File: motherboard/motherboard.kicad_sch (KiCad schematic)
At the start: 4 parts, among them J1 DF40C-100DP-0.4V(51), J2 DF40C-100DP-0.4V(51), J3 DF40C-100DP-0.4V(51), J4 DF40C-100DP-0.4V(51)

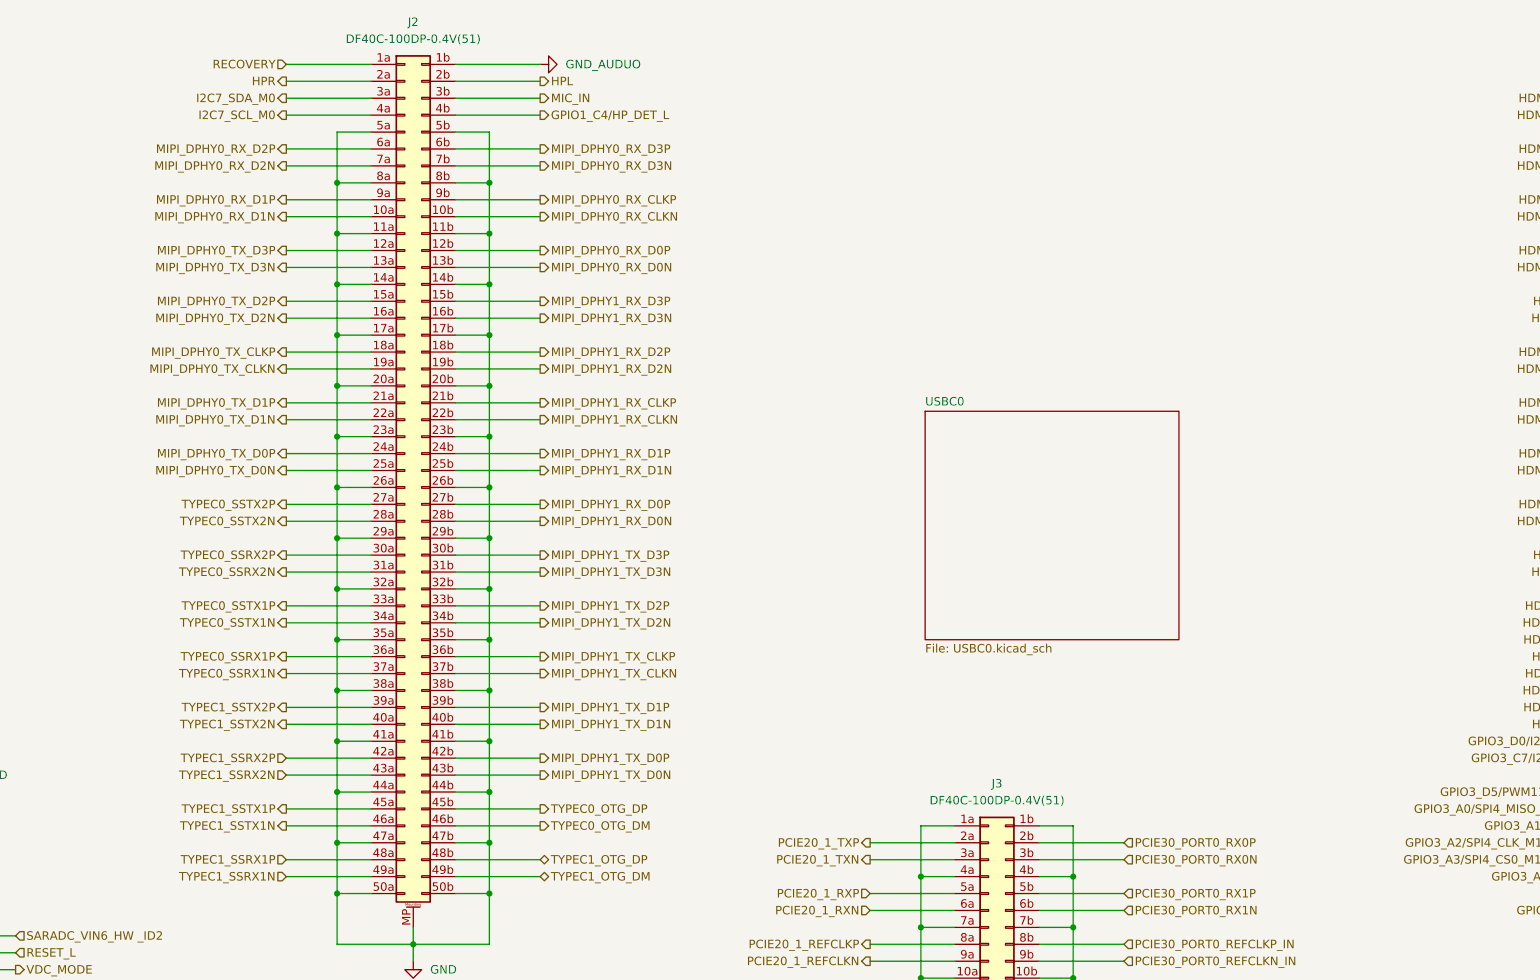
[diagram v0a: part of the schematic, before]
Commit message: hdmi, edp, peripheral implementations
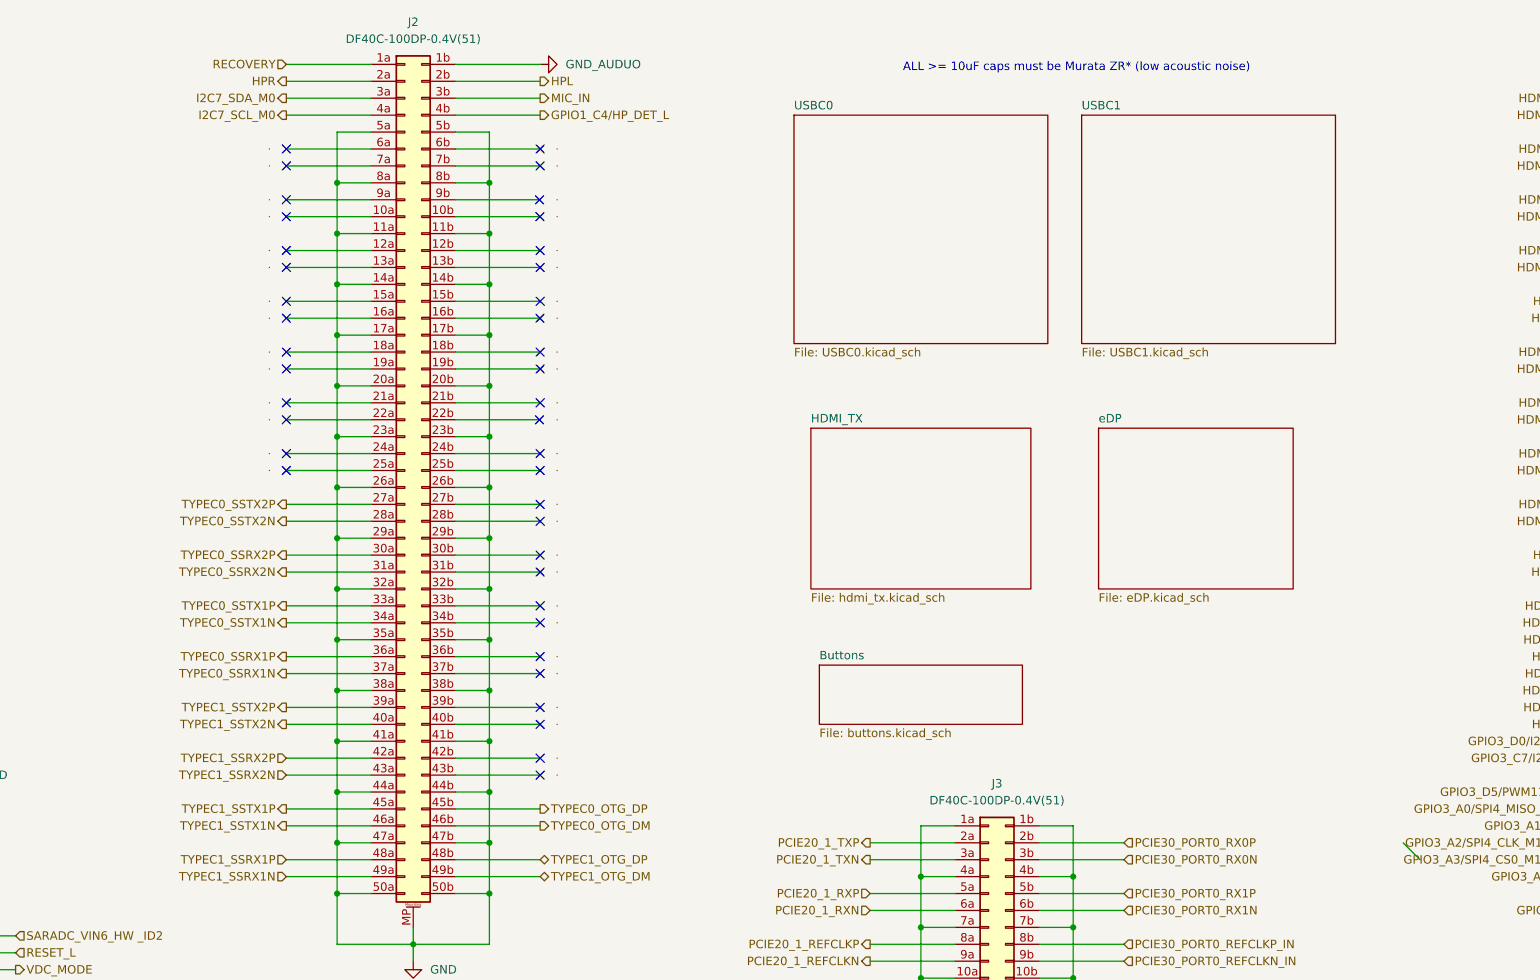
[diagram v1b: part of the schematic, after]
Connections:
- net MIPI_DPHY0_RX_CLKN: no longer J2.10b (Pin_10b)
- net MIPI_DPHY0_RX_CLKP: no longer J2.9b (Pin_9b)
- net MIPI_DPHY0_RX_D0N: no longer J2.13b (Pin_13b)
- net MIPI_DPHY0_RX_D0P: no longer J2.12b (Pin_12b)
- net MIPI_DPHY0_RX_D1N: no longer J2.10a (Pin_10a)
- net MIPI_DPHY0_RX_D1P: no longer J2.9a (Pin_9a)
- net MIPI_DPHY0_RX_D2N: no longer J2.7a (Pin_7a)
- net MIPI_DPHY0_RX_D2P: no longer J2.6a (Pin_6a)
- net MIPI_DPHY0_RX_D3N: no longer J2.7b (Pin_7b)
- net MIPI_DPHY0_RX_D3P: no longer J2.6b (Pin_6b)
- net MIPI_DPHY0_TX_CLKN: no longer J2.19a (Pin_19a)
- net MIPI_DPHY0_TX_CLKP: no longer J2.18a (Pin_18a)
- net MIPI_DPHY0_TX_D0N: no longer J2.25a (Pin_25a)
- net MIPI_DPHY0_TX_D0P: no longer J2.24a (Pin_24a)
- net MIPI_DPHY0_TX_D1N: no longer J2.22a (Pin_22a)
- net MIPI_DPHY0_TX_D1P: no longer J2.21a (Pin_21a)
- net MIPI_DPHY0_TX_D2N: no longer J2.16a (Pin_16a)
- net MIPI_DPHY0_TX_D2P: no longer J2.15a (Pin_15a)
- net MIPI_DPHY0_TX_D3N: no longer J2.13a (Pin_13a)
- net MIPI_DPHY0_TX_D3P: no longer J2.12a (Pin_12a)
- net MIPI_DPHY1_RX_CLKN: no longer J2.22b (Pin_22b)
- net MIPI_DPHY1_RX_CLKP: no longer J2.21b (Pin_21b)
- net MIPI_DPHY1_RX_D0N: no longer J2.28b (Pin_28b)
- net MIPI_DPHY1_RX_D0P: no longer J2.27b (Pin_27b)
- net MIPI_DPHY1_RX_D1N: no longer J2.25b (Pin_25b)
- net MIPI_DPHY1_RX_D1P: no longer J2.24b (Pin_24b)
- net MIPI_DPHY1_RX_D2N: no longer J2.19b (Pin_19b)
- net MIPI_DPHY1_RX_D2P: no longer J2.18b (Pin_18b)
- net MIPI_DPHY1_RX_D3N: no longer J2.16b (Pin_16b)
- net MIPI_DPHY1_RX_D3P: no longer J2.15b (Pin_15b)
- net MIPI_DPHY1_TX_CLKN: no longer J2.37b (Pin_37b)
- net MIPI_DPHY1_TX_CLKP: no longer J2.36b (Pin_36b)
- net MIPI_DPHY1_TX_D0N: no longer J2.43b (Pin_43b)
- net MIPI_DPHY1_TX_D0P: no longer J2.42b (Pin_42b)
- net MIPI_DPHY1_TX_D1N: no longer J2.40b (Pin_40b)
- net MIPI_DPHY1_TX_D1P: no longer J2.39b (Pin_39b)
- net MIPI_DPHY1_TX_D2N: no longer J2.34b (Pin_34b)
- net MIPI_DPHY1_TX_D2P: no longer J2.33b (Pin_33b)
- net MIPI_DPHY1_TX_D3N: no longer J2.31b (Pin_31b)
- net MIPI_DPHY1_TX_D3P: no longer J2.30b (Pin_30b)
- no-connect marks 0 -> 40
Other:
- added sheet Buttons (buttons.kicad_sch)
- added sheet HDMI_TX (hdmi_tx.kicad_sch)
- added sheet USBC1 (USBC1.kicad_sch)
- added sheet eDP (eDP.kicad_sch)
- note added: "ALL >= 10uF caps must be Murata ZR* (low acoustic noise)"
- company: (none) -> Byran Huang
- title: (none) -> anyon e

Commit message: wip with pcie2.0 e key, ethernet, buttons and more
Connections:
- net GPIO2_B) renamed GPIO2_B0
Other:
- added sheet Ethernet (ethernet.kicad_sch)
- added sheet PCIE2.0-EKEY (pcie20-ekey.kicad_sch)
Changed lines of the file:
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@@
 		(at 166.37 101.6)
 	)
-	(bus_entry
-		(at 295.91 142.24)
-		(size 2.54 2.54)
-		(stroke
-			(width 0)
-			(type default)
-		)
-	)
 	(wire
 		(pts
@@
 		)
 	)
-	(hierarchical_label "GPIO2_B)"
+	(hierarchical_label "GPIO2_B0"
 		(shape output)
 		(at 49.53 245.11 180)
@@
 	)
 	(sheet
+		(at 251.46 115.57)
+		(size 30.48 8.89)
+		(fields_autoplaced yes)
+		(stroke
+			(width 0.1524)
+			(type solid)
+		)
+		(fill
+			(color 0 0 0 0.0000)
+		)
+		(property "Sheetname" "PCIE2.0-EKEY"
+			(at 251.46 114.8584 0)
+			(effects
+				(font
+					(size 1.27 1.27)
+				)
+				(justify left bottom)
+			)
+		)
+		(property "Sheetfile" "pcie20-ekey.kicad_sch"
+			(at 251.46 125.0446 0)
+			(effects
+				(font
+					(size 1.27 1.27)
+				)
+				(justify left top)
+			)
+		)
+		(instances
+			(project "motherboard"
+				(path "/025fe4d1-0305-4b34-be04-f8d9818125a4"
+					(page "7")
+				)
+			)
+		)
+	)
+	(sheet
 		(at 247.65 33.02)
 		(size 38.1 34.29)
@@
 				)
 			)
+		)
+	)
+	(sheet
+		(at 137.16 173.99)
+		(size 26.67 16.51)
+		(fields_autoplaced yes)
+		(stroke
+			(width 0.1524)
+			(type solid)
+		)
+		(fill
+			(color 0 0 0 0.0000)
+		)
+		(property "Sheetname" "Ethernet"
+			(at 137.16 173.2784 0)
+			(effects
+				(font
+					(size 1.27 1.27)
+				)
+				(justify left bottom)
+			)
+		)
+		(property "Sheetfile" "ethernet.kicad_sch"
+			(at 137.16 191.0846 0)
+			(effects
+				(font
+					(size 1.27 1.27)
+				)
+				(justify left top)
+			)
+		)
+		(instances
+			(project "motherboard"
+				(path "/025fe4d1-0305-4b34-be04-f8d9818125a4"
+					(page "8")
+				)
+			)

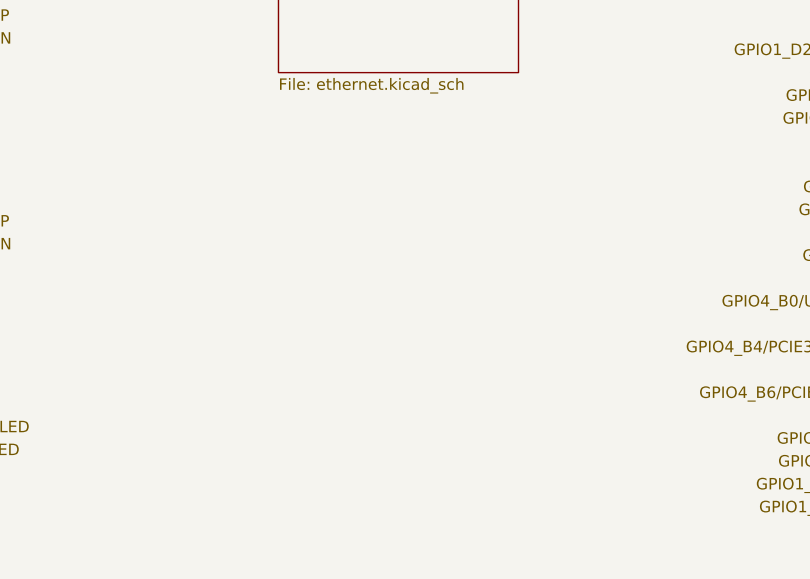
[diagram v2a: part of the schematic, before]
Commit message: haptics wip, created encoder pcb
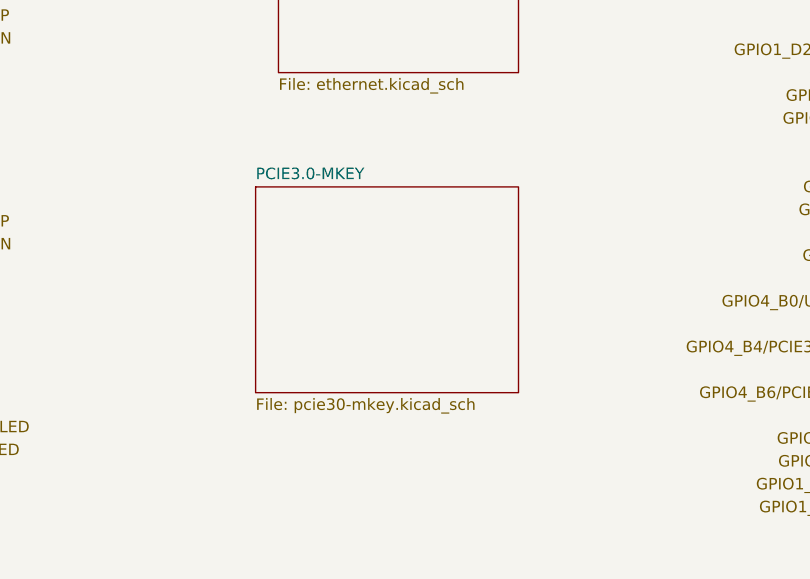
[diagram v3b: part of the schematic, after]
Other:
- added sheet PCIE3.0-MKEY (pcie30-mkey.kicad_sch)
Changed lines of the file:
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@@
+	)
+	(sheet
+		(at 134.62 203.2)
+		(size 29.21 22.86)
+		(fields_autoplaced yes)
+		(stroke
+			(width 0.1524)
+			(type solid)
+		)
+		(fill
+			(color 0 0 0 0.0000)
+		)
+		(property "Sheetname" "PCIE3.0-MKEY"
+			(at 134.62 202.4884 0)
+			(effects
+				(font
+					(size 1.27 1.27)
+				)
+				(justify left bottom)
+			)
+		)
+		(property "Sheetfile" "pcie30-mkey.kicad_sch"
+			(at 134.62 226.6446 0)
+			(effects
+				(font
+					(size 1.27 1.27)
+				)
+				(justify left top)
+			)
+		)
+		(instances
+			(project "motherboard"
+				(path "/025fe4d1-0305-4b34-be04-f8d9818125a4"
+					(page "9")
+				)
+			)
+		)
 	)
 	(sheet

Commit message: implemented most features
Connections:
- net MIPI_CSI0_RX_CLK0N: no longer J1.28b (Pin_28b)
- net MIPI_CSI0_RX_CLK0P: no longer J1.27b (Pin_27b)
- net MIPI_CSI0_RX_CLK1N: no longer J1.19b (Pin_19b)
- net MIPI_CSI0_RX_CLK1P: no longer J1.18b (Pin_18b)
- net MIPI_CSI0_RX_D0N: no longer J1.34b (Pin_34b)
- net MIPI_CSI0_RX_D0P: no longer J1.33b (Pin_33b)
- net MIPI_CSI0_RX_D1N: no longer J1.31b (Pin_31b)
- net MIPI_CSI0_RX_D1P: no longer J1.30b (Pin_30b)
- net MIPI_CSI0_RX_D2N: no longer J1.25b (Pin_25b)
- net MIPI_CSI0_RX_D2P: no longer J1.24b (Pin_24b)
- net MIPI_CSI0_RX_D3N: no longer J1.22b (Pin_22b)
- net MIPI_CSI0_RX_D3P: no longer J1.21b (Pin_21b)
- net MIPI_CSI1_RX_CLK0N: no longer J1.28a (Pin_28a)
- net MIPI_CSI1_RX_CLK0P: no longer J1.27a (Pin_27a)
- net MIPI_CSI1_RX_CLK1N: no longer J1.19a (Pin_19a)
- net MIPI_CSI1_RX_CLK1P: no longer J1.18a (Pin_18a)
- net MIPI_CSI1_RX_D0N: no longer J1.34a (Pin_34a)
- net MIPI_CSI1_RX_D0P: no longer J1.33a (Pin_33a)
- net MIPI_CSI1_RX_D1N: no longer J1.31a (Pin_31a)
- net MIPI_CSI1_RX_D1P: no longer J1.30a (Pin_30a)
- net MIPI_CSI1_RX_D2N: no longer J1.25a (Pin_25a)
- net MIPI_CSI1_RX_D2P: no longer J1.24a (Pin_24a)
- net MIPI_CSI1_RX_D3N: no longer J1.22a (Pin_22a)
- net MIPI_CSI1_RX_D3P: no longer J1.21a (Pin_21a)
- net GPIO4_B5 renamed GPIO4_B5/PCIE30X4_WAKEn_M1_L
- no-connect marks 40 -> 64
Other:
- added sheet SD Card (sdcard.kicad_sch)
- added sheet USB2.0 (usb20.kicad_sch)

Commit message: full cm3588 sym + fp + 3d
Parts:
- removed J1, J2, J3, J4: DF40C-100DP-0.4V(51), symbol Connector_Generic_MountingPin:Conn_02x50_Row_Letter_Last_MountingPin
- added J20: CM3588 Hirose Connector, symbol library:CM3588
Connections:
- net  GPIO3_C3/PWM15_IR_M0: now also J20.293
- net BOOT_SARADC_IN0: now also J20.15
- net GND: now also J20.100, J20.109, J20.11, J20.110, J20.115, J20.116, J20.12, J20.121, J20.122, J20.127, J20.128, J20.13, J20.133, J20.134, J20.139, J20.140, J20.145, J20.146, J20.151, J20.152, J20.157, J20.158, J20.163, J20.164, J20.169, J20.170, J20.175, J20.176, J20.181, J20.182, J20.187, J20.188, J20.193, J20.194, J20.199, J20.200, J20.201, J20.202, J20.207, J20.208, J20.213, J20.214, J20.219, J20.220, J20.225, J20.226, J20.231, J20.232, J20.237, J20.238, J20.24, J20.244, J20.249, J20.250, J20.256, J20.259, J20.262, J20.271, J20.284, J20.285, J20.294, J20.301, J20.302, J20.307, J20.308, J20.313, J20.314, J20.319, J20.320, J20.325, J20.326, J20.33, J20.331, J20.332, J20.337, J20.338, J20.34, J20.343, J20.344, J20.349, J20.350, J20.355, J20.361, J20.362, J20.368, J20.380, J20.383, J20.39, J20.396, J20.40, J20.45, J20.46, J20.51, J20.52, J20.57, J20.58, J20.63, J20.64, J20.69, J20.70, J20.73, J20.76, J20.77, J20.82, J20.88, J20.91, J20.94
- net GND_AUDUO: now also J20.102
- net GPIO0_A4/SDMMC_DET_L: now also J20.370
- net GPIO0_B2: now also J20.247
- net GPIO0_C4/UART0_RX_M0: now also J20.270
- net GPIO0_C5/UART0_TX_M0/PWM4_M0: now also J20.272
- net GPIO0_C6/PW M5_M1: now also J20.274
- net GPIO0_D3/CC_INT_L: now also J20.264
- net GPIO0_D4/PWM3_IR_M0: now also J20.266
- net GPIO0_D5: now also J20.268
- net GPIO1_A0/UART6_RX_M1: now also J20.273
- net GPIO1_A1/UART6_TX_M1: now also J20.275
- net GPIO1_A2/I2C4_SDA_M3_TP: now also J20.277
- net GPIO1_A3/I2C4_SCL_M3_TP: now also J20.279
- net GPIO1_A4: now also J20.281
- net GPIO1_A7: now also J20.283
- net GPIO1_B0: now also J20.276
- net GPIO1_B1/SPI0_MISO_M2: now also J20.278
- net GPIO1_B2/SPI0_MOSI_M2/UART4_RX_M2: now also J20.280
- net GPIO1_B3/SPI0_CLK_M2/UART4_TX_M2: now also J20.282
- net GPIO1_B4/SPI0_CS0_M2/UART7_RX_M2: now also J20.290
- net GPIO1_B5/SPI0_CS1_M0/UART7_TX_M2: now also J20.292
- net GPIO1_B6/MIPI_CAM1_CLKOUT: now also J20.71
- net GPIO1_B7/MIPI_CAM2_CLKOUT: now also J20.75
- net GPIO1_C0/I2C3_SDA_M0: now also J20.245
- net GPIO1_C1/I2C3_SCL_M0: now also J20.243
- net GPIO1_C4/HP_DET_L: now also J20.108
- net GPIO1_D2/TYPEC5V_PWREN_H: now also J20.239
- net GPIO1_D3/PWM1_M1: now also J20.241
- net GPIO1_D5/HDMIIRX_DET_L: now also J20.299
- net GPIO1_D6/I2C8_SCL_M2: now also J20.286
- net GPIO1_D7/I2C8_SDA_M2: now also J20.288
- net GPIO2_A6: now also J20.79
- net GPIO2_A7: now also J20.81
- net GPIO2_B0: now also J20.83
- net GPIO2_B1: now also J20.85
- net GPIO2_B2: now also J20.87
- net GPIO2_B3: now also J20.89
- net GPIO2_B4: now also J20.93
- net GPIO2_B5: now also J20.95
- net GPIO2_B6: now also J20.97
- net GPIO2_B7: now also J20.99
- net GPIO2_C0: now also J20.21
- net GPIO2_C1/MIPI_CAM2_RESET_L: now also J20.23
- net GPIO2_C2/MIPI_CAM2_PDN_L: now also J20.25
- net GPIO2_C3: now also J20.27
- net GPIO2_C4: now also J20.29
- net GPIO2_C6: now also J20.31
- net GPIO3_A0/SPI4_MISO_M1/PWM10_M0: now also J20.387
- net GPIO3_A1/SPI4_MOSI_M1: now also J20.389
- net GPIO3_A2/SPI4_CLK_M1/UART8_TX_M1: now also J20.391
- net GPIO3_A3/SPI4_CS0_M1/UART8_RX_M1: now also J20.393
- net GPIO3_A4/SPI4_CS1_M1: now also J20.395
- net GPIO3_A5: now also J20.397
- net GPIO3_A6/LCD_RST: now also J20.399
- net GPIO3_A7: now also J20.400
- net GPIO3_B0/PWM9_M0: now also J20.382
- net GPIO3_B1/PWM2_M1/LCD_BL: now also J20.384
- net GPIO3_B2: now also J20.386
- net GPIO3_B3: now also J20.388
- net GPIO3_B4: now also J20.390
- net GPIO3_B5/UART3_TX_M1/PWM12_M0: now also J20.392
- net GPIO3_B6/UART3_RX_M1/PWM13_M0: now also J20.394
- net GPIO3_B7: now also J20.398
- net GPIO3_C0/TP_INT_L: now also J20.287
- net GPIO3_C1/TP_RST_L: now also J20.289
- net GPIO3_C2/PWM14_M0: now also J20.291
- net GPIO3_C7/I2C5_SCL_M0_TP: now also J20.381
- net GPIO3_D0/I2C5_SDA_M0_TP: now also J20.379
- net GPIO3_D5/PWM11_M3/LCD_2_BL: now also J20.385
- net GPIO4_A0/TP_2_INT_L: now also J20.251
- net GPIO4_A1/TP_2_RST_L: now also J20.253
- net GPIO4_A2: now also J20.255
- net GPIO4_A3/LCD_2_RST: now also J20.257
- net GPIO4_B0/USB_HOST_PWREN_H: now also J20.261
- net GPIO4_B3: now also J20.263
- net GPIO4_B4/PCIE30X4_CLKREQn_M1_L: now also J20.265
- net GPIO4_B5/PCIE30X4_WAKEn_M1_L: now also J20.267
- net GPIO4_B6/PCIE30X4_PERSTn_M1_L: now also J20.269
- net GPIO4_C2: now also J20.26
- net GPIO4_C3: now also J20.28
- net GPIO4_C4/MIPI_CAM1_RESET_L: now also J20.30
- net GPIO4_C5/MIPI_CAM1_PDN_L: now also J20.32
- net HDMI0_TX0N_PORT: now also J20.347
- net HDMI0_TX0P_PORT: now also J20.345
- net HDMI0_TX1N_PORT: now also J20.341
- net HDMI0_TX1P_PORT: now also J20.339
- net HDMI0_TX2N_PORT: now also J20.335
- net HDMI0_TX2P_PORT: now also J20.333
- net HDMI0_TX3N_PORT: now also J20.353
- net HDMI0_TX3P_PORT: now also J20.351
- net HDMI0_TX_ON_H: now also J20.369
- net HDMI0_TX_SBDN: now also J20.359
- net HDMI0_TX_SBDP: now also J20.357
- net HDMI1_TX0N_PORT: now also J20.317
- net HDMI1_TX0P_PORT: now also J20.315
- net HDMI1_TX1N_PORT: now also J20.311
- net HDMI1_TX1P_PORT: now also J20.309
- net HDMI1_TX2N_PORT: now also J20.305
- net HDMI1_TX2P_PORT: now also J20.303
- net HDMI1_TX3N_PORT: now also J20.323
- net HDMI1_TX3P_PORT: now also J20.321
- net HDMI1_TX_ON_H: now also J20.377
- net HDMI1_TX_SBDN: now also J20.329
- net HDMI1_TX_SBDP: now also J20.327
- net HDMIIRX_HPDOUT_H: now also J20.378
- net HDMITX0_CEC_M0: now also J20.367
- net HDMITX0_HPDIN_M0: now also J20.295
- net HDMITX0_SCL_M0: now also J20.363
- net HDMITX0_SDA_M0: now also J20.365
- net HDMITX1_CEC_M2: now also J20.375
- net HDMITX1_HPDIN_M0: now also J20.297
- net HDMITX1_SCL_M1: now also J20.371
- net HDMITX1_SDA_M1: now also J20.373
- net HDMI_RX_CEC: now also J20.376
- net HDMI_RX_CLKN_PORT: now also J20.348
- net HDMI_RX_CLKP_PORT: now also J20.346
- net HDMI_RX_D0N_PORT: now also J20.342
- net HDMI_RX_D0P_PORT: now also J20.340
- net HDMI_RX_D1N_PORT: now also J20.336
- net HDMI_RX_D1P_PORT: now also J20.334
- net HDMI_RX_D2N_PORT: now also J20.330
- net HDMI_RX_D2P_PORT: now also J20.328
- net HDMI_RX_SCL_M1: now also J20.372
- net HDMI_RX_SDA_M1: now also J20.374
- net HPL: now also J20.104
- net HPR: now also J20.103
- net I2C6_SCL_M0: now also J20.296
- net I2C6_SDA_M0: now also J20.298
- net I2C7_SCL_M0: now also J20.107
- net I2C7_SDA_M0: now also J20.105
- net LED2_25GLAN_1GLED: now also J20.74
- net LED3_25GLAN_25GLED: now also J20.72
- net MIC_IN: now also J20.106
- net P25G_MDIN0: now also J20.80
- net P25G_MDIN1: now also J20.86
- net P25G_MDIN2: now also J20.92
- net P25G_MDIN3: now also J20.98
- net P25G_MDIP0: now also J20.78
- net P25G_MDIP1: now also J20.84
- net P25G_MDIP2: now also J20.90
- net P25G_MDIP3: now also J20.96
- net PCIE20_1_REFCLKN: now also J20.217
- net PCIE20_1_REFCLKP: now also J20.215
- net PCIE20_1_RXN: now also J20.211
- net PCIE20_1_RXP: now also J20.209
- net PCIE20_1_TXN: now also J20.205
- net PCIE20_1_TXP: now also J20.203
- net PCIE20_2_REFCLKN: now also J20.229
- net PCIE20_2_REFCLKP: now also J20.227
- net PCIE20_2_RXN: now also J20.223
- net PCIE20_2_RXP: now also J20.221
- net PCIE20_2_TXN: now also J20.235
- net PCIE20_2_TXP: now also J20.233
- net PCIE30_PORT0_REFCLKN_IN: now also J20.218
- net PCIE30_PORT0_REFCLKP_IN: now also J20.216
- net PCIE30_PORT0_RX0N: now also J20.206
- net PCIE30_PORT0_RX0P: now also J20.204
- net PCIE30_PORT0_RX1N: now also J20.212
- net PCIE30_PORT0_RX1P: now also J20.210
- net PCIE30_PORT0_TX0N: now also J20.224
- net PCIE30_PORT0_TX0P: now also J20.222
- net PCIE30_PORT0_TX1N: now also J20.230
- net PCIE30_PORT0_TX1P: now also J20.228
- net PCIE30_PORT1_REFCLKN_IN: now also J20.260
- net PCIE30_PORT1_REFCLKP_IN: now also J20.258
- net PCIE30_PORT1_RX2N: now also J20.236
- net PCIE30_PORT1_RX2P: now also J20.234
- net PCIE30_PORT1_RX3N: now also J20.242
- net PCIE30_PORT1_RX3P: now also J20.240
- net PCIE30_PORT1_TX2N: now also J20.248
- net PCIE30_PORT1_TX2P: now also J20.246
- net PCIE30_PORT1_TX3N: now also J20.254
- net PCIE30_PORT1_TX3P: now also J20.252
- net PMIC_EXT_EN_OUT: now also J20.19
- net PWRON_L: now also J20.17
- net RECOVERY: now also J20.101
- net RESET_L: now also J20.16
- net SARADC_VIN6_HW _ID2: now also J20.14
- net SDMMC0_CMD: now also J20.356
- net SDMMC0_D0: now also J20.364
- net SDMMC0_D1: now also J20.366
- net SDMMC0_D2: now also J20.352
- net SDMMC0_D3: now also J20.354
- net SD_CLK: now also J20.360
- net TYPEC0_OTG_DM: now also J20.192
- net TYPEC0_OTG_DP: now also J20.190
- net TYPEC0_SBU1_OUT: now also J20.304
- net TYPEC0_SBU2_OUT: now also J20.306
- net TYPEC0_SSRX1N: now also J20.173
- net TYPEC0_SSRX1P: now also J20.171
- net TYPEC0_SSRX2N: now also J20.161
- net TYPEC0_SSRX2P: now also J20.159
- net TYPEC0_SSTX1N: now also J20.167
- net TYPEC0_SSTX1P: now also J20.165
- net TYPEC0_SSTX2N: now also J20.155
- net TYPEC0_SSTX2P: now also J20.153
- net TYPEC1_OTG_DM: now also J20.198
- net TYPEC1_OTG_DP: now also J20.196
- net TYPEC1_SBU1: now also J20.310
- net TYPEC1_SBU2: now also J20.312
- net TYPEC1_SSRX1N: now also J20.197
- net TYPEC1_SSRX1P: now also J20.195
- net TYPEC1_SSRX2N: now also J20.185
- net TYPEC1_SSRX2P: now also J20.183
- net TYPEC1_SSTX1N: now also J20.191
- net TYPEC1_SSTX1P: now also J20.189
- net TYPEC1_SSTX2N: now also J20.179
- net TYPEC1_SSTX2P: now also J20.177
- net UART2_RX_M0_DEBUG: now also J20.22
- net UART2_TX_M0_DEBUG: now also J20.20
- net USB20_HOST0_DM: now also J20.324
- net USB20_HOST0_DP: now also J20.322
- net USB20_HOST1_DM: now also J20.318
- net USB20_HOST1_DP: now also J20.316
- net VBAT_RTC: now also J20.300
- net VCC3V3_SD_S0: now also J20.358
- net VDC_MODE: now also J20.18
- net VDD: now also J20.1, J20.10, J20.2, J20.3, J20.4, J20.5, J20.6, J20.7, J20.8, J20.9

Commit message: synchronizing hierarchical pins
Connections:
- net SARADC_VIN6_HW _ID2 renamed SARADC_VIN6_HW_ID2
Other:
- sheet Buttons renamed System
- sheet Ethernet ports: added LED2_25GLAN_1GLED, LED3_25GLAN_25GLED, P25G_MDIN0, P25G_MDIN1, P25G_MDIN2, P25G_MDIN3, P25G_MDIP0, P25G_MDIP1, P25G_MDIP2, P25G_MDIP3; removed none
- sheet HDMI_TX ports: added HDMI0_TX0N_PORT, HDMI0_TX0P_PORT, HDMI0_TX1N_PORT, HDMI0_TX1P_PORT, HDMI0_TX2N_PORT, HDMI0_TX2P_PORT, HDMI0_TX3N_PORT, HDMI0_TX3P_PORT, HDMI0_TX_ON_H, HDMI0_TX_SBDN, HDMI0_TX_SBDP, HDMITX0_CECM0, HDMITX0_HPDIN_M0, HDMITX0_SCL_M0, HDMITX0_SDA_M0; removed none
- sheet PCIE2.0-EKEY ports: added GPIO0_B2/SDIO_WAKE, GPIO0_C4/SDIO_RESET, GPIO0_C5/UART_WAKE, GPIO1_A0/UART6_RX_M1, GPIO1_A1/UART6_TX_M1, GPIO1_A2/UART_RTS, GPIO1_A3/UART_CTS, GPIO2_A6/SDIO_DATA0, GPIO2_A7/SDIO_DATA1, GPIO2_B0/SDIO_DATA2, GPIO2_B1/SDIO_DATA3, GPIO2_B2/SDIO_CMD, GPIO2_B3/SDIO_CLK, GPIO2_B7/PCM_CLK/I2S_SCK, GPIO2_C0/PCM_SYNC/I2S_WS, GPIO2_C3/PCM_IN/I2S_SD_IN, GPIO3_A6/VENDOR_DEFINED, GPIO4_A0/CLKREQ0, GPIO4_A1/PEWAKE0, GPIO4_A2/PERST0, GPIO4_C3/PCM_OUT/I2S_SD_OUT, PCIE20_1_REFCLKN, PCIE20_1_REFCLKP, PCIE20_1_RXN, PCIE20_1_RXP, PCIE20_1_TXN, PCIE20_1_TXP, USB_PCIE20_DN, USB_PCIE20_DP; removed none
- sheet PCIE3.0-MKEY ports: added GPIO4_B4/PCIE30X4_CLKREQn_M1_L, GPIO4_B5/PCIE30X4_WAKEn_M1_L, GPIO4_B6/PCIE30X4_PERSTn_M1_L, PCIE0_PORT0_REFCLKN_IN, PCIE0_PORT0_REFCLKP_IN, PCIE0_PORT1_REFCLKN_IN, PCIE0_PORT1_REFCLKP_IN, PCIE30_PORT0_RX0N, PCIE30_PORT0_RX0P, PCIE30_PORT0_RX1N, PCIE30_PORT0_RX1P, PCIE30_PORT0_TX0N, PCIE30_PORT0_TX0P, PCIE30_PORT0_TX1N, PCIE30_PORT0_TX1P, PCIE30_PORT1_RX2N, PCIE30_PORT1_RX2P, PCIE30_PORT1_RX3N, PCIE30_PORT1_RX3P, PCIE30_PORT1_TX2N, PCIE30_PORT1_TX2P, PCIE30_PORT1_TX3N, PCIE30_PORT1_TX3P; removed none
- sheet SD Card ports: added GPIO0_A4/SDMMC_DET_L, SDMMC0_CMD, SDMMC0_D0, SDMMC0_D1, SDMMC0_D2, SDMMC0_D3, SD_CLK, VCC3V3_SD_S0; removed none
- sheet System: file buttons.kicad_sch -> system.kicad_sch
- sheet System ports: added BOOT_SARADC_IN0, GPIO1_D3/PWM1_M1, PWRON_L, RECOVERY, RESET_L, UART2_RX_M0_DEBUG, UART2_TX_M0_DEBUG, VBAT_RTC, VDC_MODE; removed none
- sheet USB2.0 ports: added D+, D-, DM1, DP1, USB20_HOST1_DM, USB20_HOST1_DP; removed none
- sheet USBC0 ports: added D+, D-, FUSB_INT, FUSB_SCL, FUSB_SDA, GPIO1_D2/TYPEC5V_PWREN_H, RX1+, RX1-, RX2+, RX2-, SBUS1, SBUS2, TX1+, TX1-, TX2+, TX2-, VBUS; removed none
- sheet USBC1 ports: added D+, D-, FUSB_INT, FUSB_SCL, FUSB_SDA, GPIO1_D2/TYPEC5V_PWREN_H, RX1+, RX1-, RX2+, RX2-, SBUS1, SBUS2, TX1+, TX1-, TX2+, TX2-, VBUS; removed none

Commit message: linked all footprints
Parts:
- J20: footprint (none) -> Library:CM3588
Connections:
- no-connect marks 64 -> 66
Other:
- note added: "2k2 pull up device side"
- note added: "5-20V input, 20w max"
- note added: "custom selected gpio"
- moved on the sheet: J20A, J20B, J20C, J20D
